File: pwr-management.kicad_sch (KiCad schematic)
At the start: 24 parts, among them IC1 BQ25176JDSGR, Q1 NMOS, Q2 NMOS, U1 BQ297xy, U2 MCP1640Bx-xCHY, U3 MCP1727-0802xSN

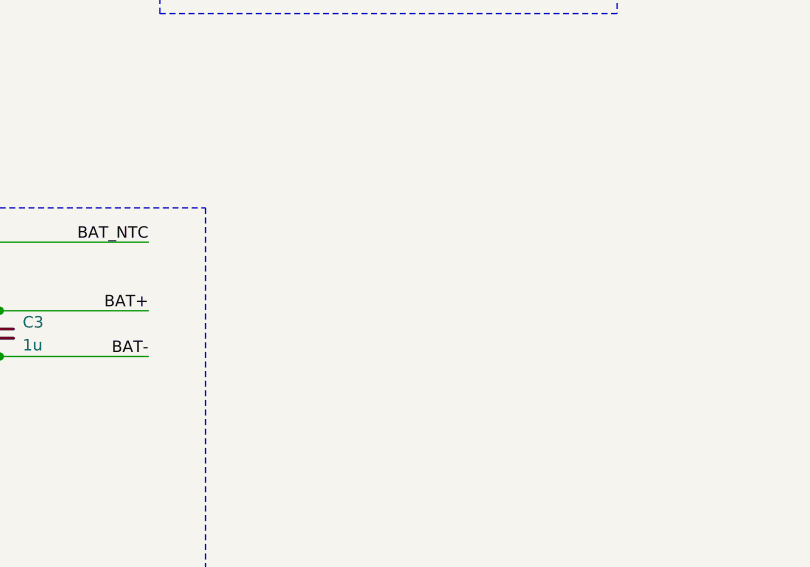
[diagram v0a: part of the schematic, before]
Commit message: component routing
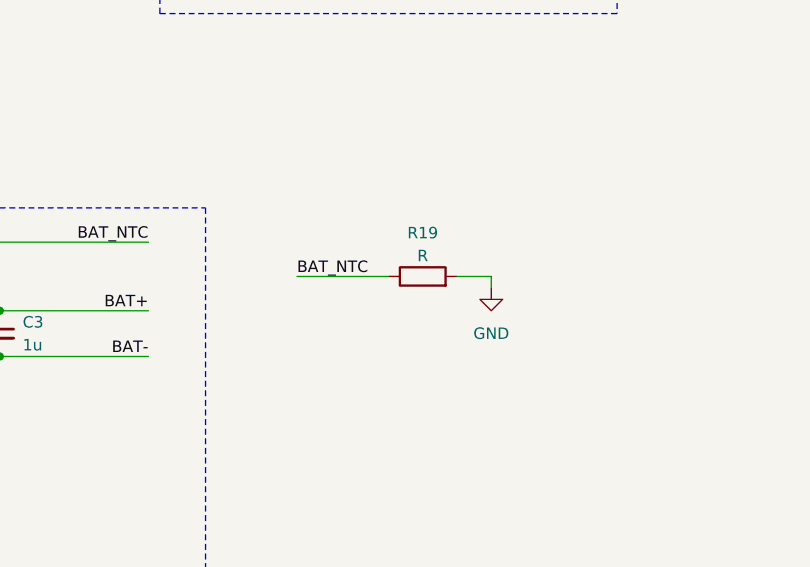
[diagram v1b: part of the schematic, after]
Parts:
- added R19: R, symbol Device:R
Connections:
- net BAT_NTC: now also R19.1
- net GND: now also R19.2
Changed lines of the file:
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@@
+	(wire
+		(pts
+			(xy 187.96 106.68) (xy 187.96 107.95)
+		)
+		(stroke
+			(width 0)
+			(type default)
+		)
+	)
 	(wire
 		(pts
@@
 	(wire
 		(pts
+			(xy 166.37 106.68) (xy 176.53 106.68)
+		)
+		(stroke
+			(width 0)
+			(type default)
+		)
+	)
+	(wire
+		(pts
 			(xy 191.77 69.85) (xy 191.77 66.04)
 		)
@@
 		(pts
 			(xy 54.61 142.24) (xy 38.1 142.24)
+		)
+		(stroke
+			(width 0)
+			(type default)
+		)
+	)
+	(wire
+		(pts
+			(xy 184.15 106.68) (xy 187.96 106.68)
 		)
 		(stroke
@@
 			)
 			(justify right bottom)
+		)
+	)
+	(label "BAT_NTC"
+		(at 166.37 106.68 0)
+		(effects
+			(font
+				(size 1.27 1.27)
+			)
+			(justify left bottom)
 		)
 	)
@@
 	)
 	(symbol
+		(lib_id "Device:R")
+		(at 180.34 106.68 90)
+		(unit 1)
+		(exclude_from_sim no)
+		(in_bom yes)
+		(on_board yes)
+		(dnp no)
+		(property "Reference" "R19"
+			(at 180.34 101.854 90)
+			(effects
+				(font
+					(size 1.27 1.27)
+				)
+			)
+		)
+		(property "Value" "R"
+			(at 180.34 104.394 90)
+			(effects
+				(font
+					(size 1.27 1.27)
+				)
+			)
+		)
+		(property "Footprint" ""
+			(at 180.34 108.458 90)
+			(effects
+				(font
+					(size 1.27 1.27)
+				)
+				(hide yes)
+			)
+		)
+		(property "Datasheet" "~"
+			(at 180.34 106.68 0)
+			(effects
+				(font
+					(size 1.27 1.27)
+				)
+				(hide yes)
+			)
+		)
+		(property "Description" "Resistor"
+			(at 180.34 106.68 0)
+			(effects
+				(font
+					(size 1.27 1.27)
+				)
+				(hide yes)
+			)
+		)
+		(pin "2"
+		)
+		(pin "1"
+		)
+		(instances
+			(project ""
+				(path "/3130e1f2-bde1-4b12-bd54-0e1e50bd36da/ab6e6673-c97f-4978-8f9b-ae71c723cdfa"
+					(reference "R19")
+					(unit 1)
+				)
+			)
+		)
+	)
+	(symbol
 		(lib_id "Device:C")
 		(at 191.77 62.23 0)
@@
 					(unit 1)
 				)
+			)
+		)
+	)
+	(symbol
+		(lib_id "power:GND")
+		(at 187.96 107.95 0)
+		(unit 1)
+		(exclude_from_sim no)
+		(in_bom yes)
+		(on_board yes)
+		(dnp no)
+		(fields_autoplaced yes)
+		(property "Reference" "#PWR048"
+			(at 187.96 114.3 0)
+			(effects
+				(font
+					(size 1.27 1.27)
+				)
+				(hide yes)
+			)
+		)
+		(property "Value" "GND"
+			(at 187.96 113.03 0)
+			(effects
+				(font
+					(size 1.27 1.27)
+				)
+			)
+		)
+		(property "Footprint" ""
+			(at 187.96 107.95 0)
+			(effects
+				(font
+					(size 1.27 1.27)
+				)
+				(hide yes)
+			)
+		)
+		(property "Datasheet" ""
+			(at 187.96 107.95 0)
+			(effects
+				(font
+					(size 1.27 1.27)
+				)
+				(hide yes)
+			)
+		)
+		(property "Description" "Power symbol creates a global label with name \"GND\" , ground"
+			(at 187.96 107.95 0)
+			(effects
+				(font
+					(size 1.27 1.27)
+				)
+				(hide yes)
+			)
+		)
+		(pin "1"
+		)
+		(instances
+			(project ""
+				(path "/3130e1f2-bde1-4b12-bd54-0e1e50bd36da/ab6e6673-c97f-4978-8f9b-ae71c723cdfa"
+					(reference "#PWR048")
+					(unit 1)
+				)

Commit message: add resistor footprint
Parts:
- R19: footprint (none) -> Resistor_SMD:R_0603_1608Metric
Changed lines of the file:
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@@
 			)
 		)
-		(property "Footprint" ""
+		(property "Footprint" "Resistor_SMD:R_0603_1608Metric"
 			(at 180.34 108.458 90)
 			(effects

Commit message: LUIGI
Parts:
- C23, C24: value C -> 10u
- R10: value R_Small -> 562
- R19: value R -> 10k
- R9: value R_Small -> 976
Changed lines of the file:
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@@
 			)
 		)
-		(property "Value" "R"
+		(property "Value" "10k"
 			(at 180.34 104.394 90)
 			(effects
@@
 			)
 		)
-		(property "Value" "C"
+		(property "Value" "10u"
 			(at 195.58 63.4999 0)
 			(effects
@@
 			)
 		)
-		(property "Value" "R_Small"
+		(property "Value" "562"
 			(at 187.96 67.3099 0)
 			(effects
@@
 			)
 		)
-		(property "Value" "C"
+		(property "Value" "10u"
 			(at 259.08 57.1499 0)
 			(effects
@@
 			)
 		)
-		(property "Value" "R_Small"
+		(property "Value" "976"
 			(at 187.96 62.2299 0)
 			(effects
